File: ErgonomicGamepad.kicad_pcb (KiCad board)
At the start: 2 copper layers, 84 parts, among them J1 USB_C_Receptacle_USB2.0_16P, J2 Conn_01x08, J3 Conn_01x08, J4 Conn_01x08, J5 AVR-ISP-6, J6 Conn_01x08, J7 1824417, SW01 SW_DIP_x01, SW02 SW_DIP_x01, SW03 SW_DIP_x01, SW04 SW_DIP_x01, SW05 SW_DIP_x01, SW06 SW_DIP_x01, SW07 SW_DIP_x01, SW08 SW_DIP_x01, SW09 SW_DIP_x01, SW10 SW_DIP_x01, SW11 SW_DIP_x01, SW12 SW_DIP_x01, SW13 SW_DIP_x01, SW14 SW_DIP_x01, SW15 SW_DIP_x01, SW16 SW_DIP_x01, SW17 SW_DIP_x01, SW18 SW_DIP_x01, SW19 SW_DIP_x01, SW20 SW_DIP_x01, SW21 SW_DIP_x01, SW22 SW_DIP_x01, SW23 SW_DIP_x01, SW24 SW_DIP_x01, U1 ATmega32U4-A, U2 USBLC6-2SC6, Y1 Crystal

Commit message: schematic+pcb: specify J2/J3/J4/J6 headers, match connector pinouts
Backfill Manufacturer (Ckmtw), MPN (B-2100S08P-A110), LCSC (C124381),
and datasheet for the J2/J3/J4/J6 edge-connector headers - confirmed
through-hole (thru_hole pads), matching the existing vertical
PinHeader footprint.

Reorient all four connectors to a consistent, matched pin-to-signal
mapping (ROW1-4 on pins 3-6, COL1 on pin 7 across all of them,
previously J4/J6 were mirrored relative to J2/J3) so a standard
straight ribbon cable works without needing a reversed/twisted crimp.
Verified via netlist export and a clean ERC pass.

Co-Authored-By: Claude Sonnet 5 <noreply@anthropic.com>
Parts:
- added J3: Conn_01x08, Connector_PinHeader_2.54mm:PinHeader_1x08_P2.54mm_Vertical, F.Cu at (166.8, 31.8)
- added J4: Conn_01x08, Connector_PinHeader_2.54mm:PinHeader_1x08_P2.54mm_Vertical, F.Cu at (171.4, 31.8)
- added J6: Conn_01x08, Connector_PinHeader_2.54mm:PinHeader_1x08_P2.54mm_Vertical, F.Cu at (176.0, 31.8)

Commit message: Remove dangling ground symbols on DNP J2/J3/J4/J6 connectors
Connectors and wiring are now properly specified: unused ROW/COLL
pins carry no-connect flags to satisfy ERC, and the stray GND
symbols left over from the JST-XH swap are deleted. PCB footprints
resynced from schematic to match.

Co-Authored-By: Claude Sonnet 5 <noreply@anthropic.com>
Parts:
- J2, J3, J4, J6: value Conn_01x08 -> Conn_01x05; footprint Connector_PinHeader_2.54mm:PinHeader_1x08_P2.54mm_Vertical -> Connector_JST:JST_XH_B5B-XH-A_1x05_P2.50mm_Vertical
- SWR1: value SW_Push -> B3U-3000P; footprint Button_Switch_SMD:SW_SPST_TL3342 -> Button_Switch_SMD:SW_SPST_B3U-3000P
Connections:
- J2 pad 1: +5V -> /ROW1
- J2 pad 2: unconnected-(J2-Pin_2-Pad2) -> /ROW2
- J2 pad 3: /ROW1 -> /ROW3
- J2 pad 4: /ROW2 -> /ROW4
- J2 pad 5: /ROW3 -> /COL1
- J3 pad 1: +5V -> /ROW1
- J3 pad 2: unconnected-(J3-Pin_2-Pad2) -> /ROW2
- J3 pad 3: /ROW1 -> /ROW3
- J3 pad 4: /ROW2 -> /ROW4
- J3 pad 5: /ROW3 -> /COL1
- J4 pad 1: +5V -> /ROW1
- J4 pad 2: unconnected-(J4-Pin_2-Pad2) -> /ROW2
- J4 pad 3: /ROW1 -> /ROW3
- J4 pad 4: /ROW2 -> /ROW4
- J4 pad 5: /ROW3 -> /COL1
- J6 pad 1: +5V -> /ROW1
- J6 pad 2: unconnected-(J6-Pin_2-Pad2) -> /ROW2
- J6 pad 3: /ROW1 -> /ROW3
- J6 pad 4: /ROW2 -> /ROW4
- J6 pad 5: /ROW3 -> /COL1

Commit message: Mirror footprint placement from schematic and fill JST connector datasheets
Add scripts/mirror_schematic_layout.py to copy footprint position/rotation
from the schematic onto the PCB (respecting locked footprints and nets that
already have routed copper), plus lock-all/unlock-all helpers for freezing a
placement pass before adding new parts. Also fill in the Datasheet field for
J2/J3/J4/J6 (JST XH B5B-XH-A, LCSC C157991).

Co-Authored-By: Claude Sonnet 5 <noreply@anthropic.com>
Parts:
- removed the J3 at (125.1, 147.9)
- removed the J3 at (166.8, 31.8)
- removed the J4 at (171.4, 31.8)
- removed the J4 at (129.7, 147.9)
- removed the J6 at (176.0, 31.8)
- removed the J6 at (134.3, 147.9)
- added J3: Conn_01x05, Connector_JST:JST_XH_B5B-XH-A_1x05_P2.50mm_Vertical, F.Cu at (59.7, 146.1)
- added J4: Conn_01x05, Connector_JST:JST_XH_B5B-XH-A_1x05_P2.50mm_Vertical, F.Cu at (39.4, 176.5)
- added J6: Conn_01x05, Connector_JST:JST_XH_B5B-XH-A_1x05_P2.50mm_Vertical, F.Cu at (59.7, 176.5)
- moved SW21 239.5 mm to (322.6, 69.8)
- moved DM21 236.7 mm to (330.2, 73.7), turned to 90 degrees
- moved DM22 230.6 mm to (330.2, 96.5), turned to 90 degrees
- moved DM23 225.9 mm to (330.2, 119.4), turned to 90 degrees
- moved DM17 223.2 mm to (298.4, 73.7), turned to 90 degrees
- moved DM09 222.4 mm to (233.7, 73.7), turned to 90 degrees
- moved DM24 221.7 mm to (328.9, 141.0), turned to 90 degrees
- moved SW24 219.2 mm to (321.3, 137.2)
- moved SW23 218.9 mm to (322.6, 115.6)
- moved SW22 217.2 mm to (322.6, 92.7)
- moved SW17 197.4 mm to (290.8, 69.8)
- moved SW19 197.3 mm to (290.8, 115.6)
- moved SW18 197.2 mm to (290.8, 92.7)
- moved SW20 196.3 mm to (289.6, 137.2)
- moved DM18 196.2 mm to (298.4, 96.5), turned to 90 degrees
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
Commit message: Fill JST connector sourcing fields, refresh production reports, and lock USB-C decisions
- J2/J3/J4/J6: fill Manufacturer/MPN/Supplier/LCSC (JST B5B-XH-A(LF)(SN), C157991)
- Regenerate jlc_sourcing_bom_template.csv from current schematic state
- Rename jlc_stock_check_queue.csv -> verify_stock_before_ordering.csv and
  repurpose it as a pre-order stock/sourcing risk checklist now that all
  parts carry LCSC numbers
- Remove stale current_sch_fields.csv scratch export
- Regenerate erc-report.rpt and drc-report.rpt against current schematic/PCB
- Document resolved USB-C implementation (reversible orientation, CC
  pulldowns, ESD array, shield grounding, power-path gating) in README
- Update PROCESS.md checklist to reflect completed sourcing and USB-C
  requirements-freeze items
- Remove stray untracked-from-disk files (M1.kicad_sch, "Original
  ErgonomicGamepad.kicad_sch", "Was ErgonomicGamepad.kicad_sch", "checked
  PROCESS.md")
- Include in-progress PCB footprint placement updates

Co-Authored-By: Claude Sonnet 5 <noreply@anthropic.com>
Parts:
- moved JP2 130.7 mm to (42.0, 35.2)
- moved R8 130.7 mm to (21.7, 35.2)
- moved LED1 129.2 mm to (28.3, 160.4)
- moved LED2 129.2 mm to (28.3, 168.0)
- moved R6 129.2 mm to (16.9, 160.4)
- moved R7 129.2 mm to (16.9, 168.0)
- moved C1 113.0 mm to (-40.4, 65.0)
- moved C2 113.0 mm to (-40.4, 72.6)
- moved C3 113.0 mm to (-44.2, 56.1)
- moved C4 113.0 mm to (-86.1, 47.2)
- moved C5 113.0 mm to (-70.9, 47.2)
- moved D1 113.0 mm to (-58.2, 67.6)
- moved J1 113.0 mm to (-79.8, 90.4)
- moved J2 113.0 mm to (-73.4, 138.7)
- moved J3 113.0 mm to (-53.1, 138.7)
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
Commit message: Add TP8/TP9 power-rail test points, group keys, and arrange all 24 on a 20mm grid
- Add TP8 (+5V) / TP9 (GND) edge-mounted clip test points via schematic +
  Update PCB from Schematic, using a 3mm THT pad footprint suited to
  alligator/hook clips (distinct from TP1-7's fine-probe pads); document
  the split in README
- Establish SW01/DM01 as the validated "key" placement template: diode
  clear of the socket courtyard, correct cathode-to-column orientation,
  connecting trace routed, silkscreen labels matching the rest of the board
- Add 03_apply_key_template.py to replicate that template's relative
  offset/rotation/trace onto SW02-24/DM02-24, including a fix for pads that
  carry their own explicit rotation (previously left stale, misaligning
  copper relative to the rotated body)
- Add 04_group_keys.py to group each SW0N/DM0N pair with its connecting
  trace into a named KeyNN group, matching the existing Key01 grouping
- Add 05_grid_keys.py to arrange all 24 keys on a uniform grid (default
  20mm pitch), rebuilding each key's diode position/rotation and trace
  from the template, and updating each KeyNN group's members to match;
  fixes an off-by-one in segment deletion and a missing-space bug in the
  group-members rewrite, found via DRC/paren-balance verification after
  the first run corrupted the file
- Renumber scripts/ with 01-05 prefixes reflecting invention/workflow order
- Regenerate erc-report.rpt and drc-report.rpt against the final state

Co-Authored-By: Claude Sonnet 5 <noreply@anthropic.com>
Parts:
- added TP8: TestPoint, TestPoint:TestPoint_THTPad_D3.0mm_Drill1.5mm, F.Cu at (201.9, 170.3)
- added TP9: TestPoint, TestPoint:TestPoint_THTPad_D3.0mm_Drill1.5mm, F.Cu at (201.9, 185.5)
- moved JP2 130.7 mm to (172.7, 36.9)
- moved R8 130.7 mm to (152.4, 36.9)
- moved LED1 129.2 mm to (157.4, 157.6)
- moved LED2 129.2 mm to (157.4, 165.2)
- moved R6 129.2 mm to (146.0, 157.6)
- moved R7 129.2 mm to (146.0, 165.2)
- moved C3 113.0 mm to (68.5, 63.6)
- moved C5 113.0 mm to (41.9, 54.7)
- moved D1 113.0 mm to (54.6, 75.0)
- moved J1 113.0 mm to (33.0, 97.9)
- moved J3 113.0 mm to (59.6, 146.1)
- moved J5 113.0 mm to (119.3, 45.8)
- moved J6 113.0 mm to (59.6, 176.6)
- moved JP1 113.0 mm to (54.6, 52.1)
- moved R3 113.0 mm to (73.6, 43.3)
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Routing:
- net Net-(DM20-A): track 0.00 -> 6.51 mm
- net Net-(DM19-A): track 0.00 -> 6.51 mm
- net Net-(DM18-A): track 0.00 -> 6.51 mm
- net Net-(DM17-A): track 0.00 -> 6.51 mm
- net Net-(DM16-A): track 0.00 -> 6.51 mm
- net Net-(DM15-A): track 0.00 -> 6.51 mm
- net Net-(DM14-A): track 0.00 -> 6.51 mm
- net Net-(DM13-A): track 0.00 -> 6.51 mm
- net Net-(DM12-A): track 0.00 -> 6.51 mm
- net Net-(DM11-A): track 0.00 -> 6.51 mm
- net Net-(DM10-A): track 0.00 -> 6.51 mm
- net Net-(DM09-A): track 0.00 -> 6.51 mm
- net Net-(DM08-A): track 0.00 -> 6.51 mm
- net Net-(DM07-A): track 0.00 -> 6.51 mm
- net Net-(DM06-A): track 0.00 -> 6.51 mm
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
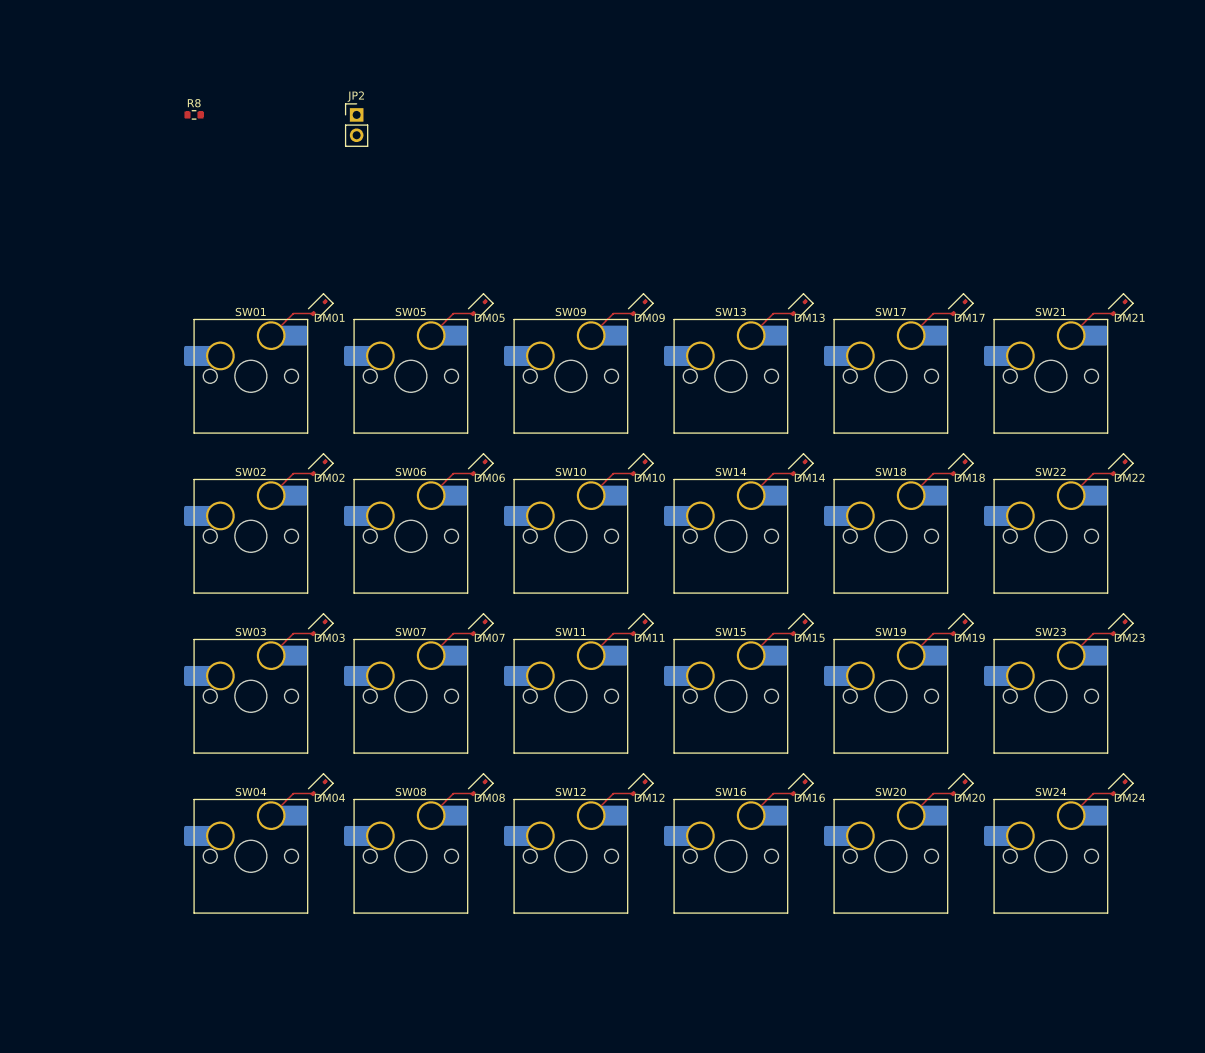
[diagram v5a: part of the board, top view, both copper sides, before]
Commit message: Add key move/align scripts and begin ergonomic stagger adjustments
- Add 06_move_key.py: translate a whole key (switch + diode + connecting
  trace) up/down/left/right by a specified distance - a pure translation,
  so no pad-angle fix is needed (unlike 03/05's rotated diode placement)
- Add 07_align_key.py: move one key to match another's X or Y exactly,
  computing the required delta automatically rather than taking a
  specified distance
- Relocate Key01/Key02/Key04 (column 1, rows 1/2/4) into their own
  offset row toward the lower-right, and nudge Key17-20/Key21-24 and the
  whole board per iterative ergonomic placement adjustments
- Regenerate drc-report.rpt against the current placement (62 violations,
  145 unconnected - unchanged from pre-adjustment baseline aside from
  position; 0 courtyard overlaps throughout)

Column 1's split placement (SW03 left behind while SW01/02/04 moved) and
SW21's displacement from its row/column neighbors both introduce ~75-80mm
ratsnest jumps for ROW1/COL1 - confirmed still routable, just longer runs
than the rest of the grid.

Co-Authored-By: Claude Sonnet 5 <noreply@anthropic.com>
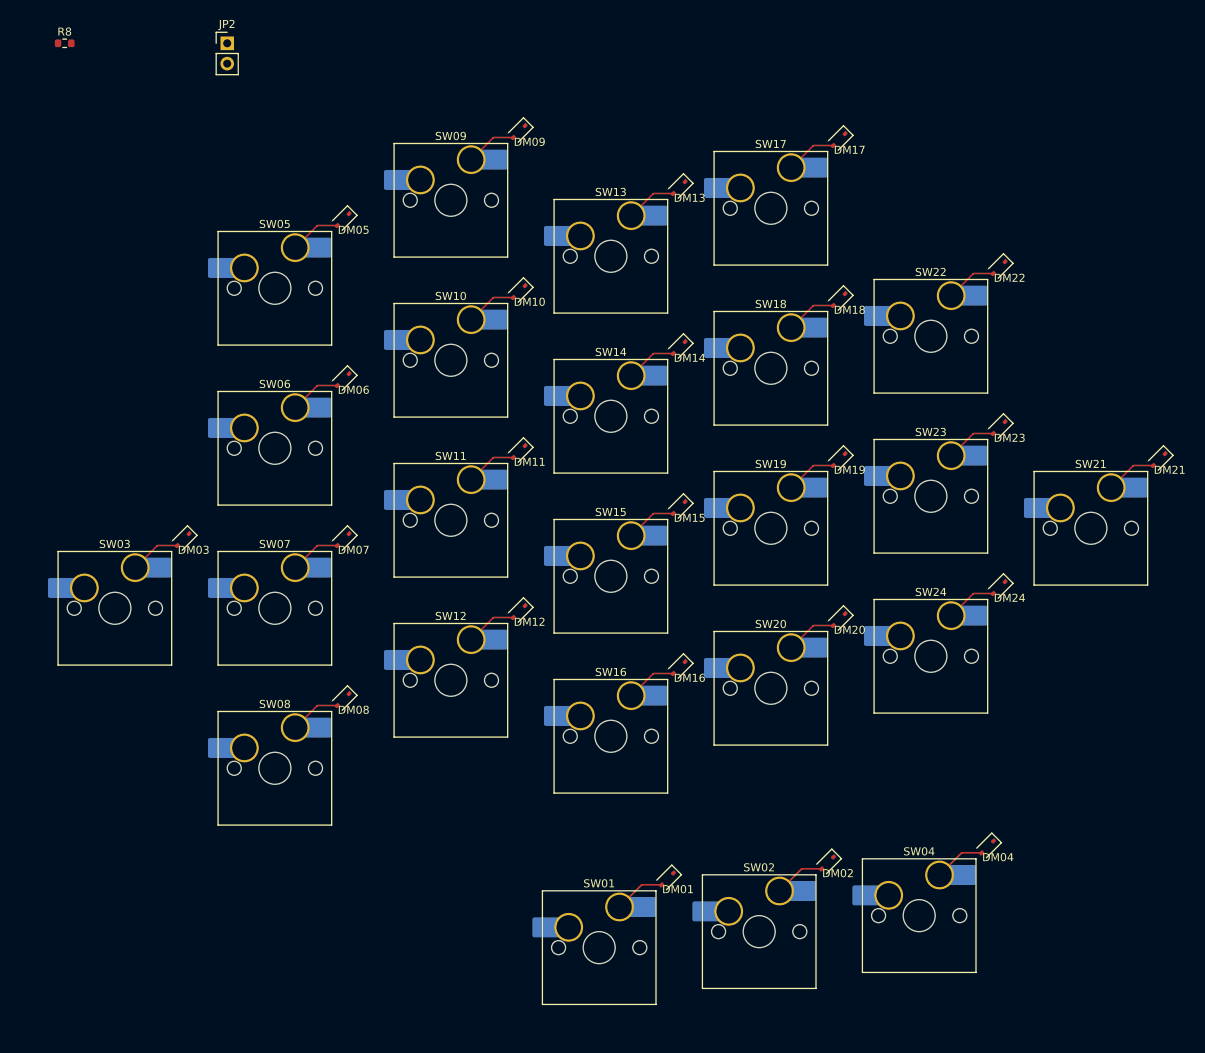
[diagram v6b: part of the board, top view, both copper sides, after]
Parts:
- moved DM04 83.9 mm to (251.5, 128.4)
- moved SW04 83.9 mm to (243.0, 137.0)
- moved SW01 83.6 mm to (203.0, 141.0)
- moved DM01 83.6 mm to (211.5, 132.4)
- moved DM02 80.5 mm to (231.5, 130.4)
- moved SW02 80.5 mm to (223.0, 139.0)
- moved DM22 29.2 mm to (253.0, 56.0)
- moved DM23 29.2 mm to (253.0, 76.0)
- moved DM24 29.2 mm to (253.0, 96.0)
- moved SW24 29.2 mm to (244.5, 104.6)
- moved SW22 29.2 mm to (244.5, 64.6)
- moved SW23 29.2 mm to (244.5, 84.6)
- moved SW12 26.6 mm to (184.5, 107.6)
- moved DM09 26.6 mm to (193.0, 39.0)
- moved DM10 26.6 mm to (193.0, 59.0)
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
